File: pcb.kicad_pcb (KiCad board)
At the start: 2 copper layers, 40.6 x 40.6 mm, 3 parts

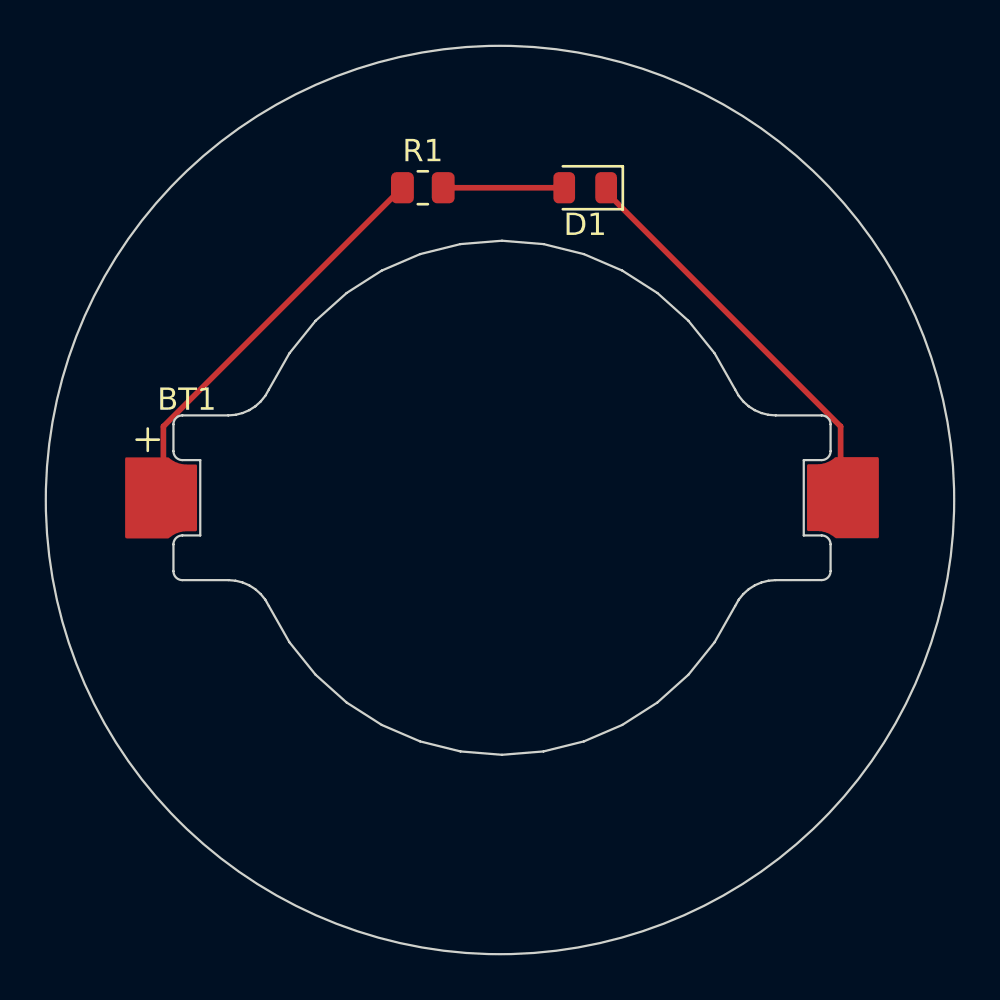
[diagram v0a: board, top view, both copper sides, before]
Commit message: hopefully fix example :/
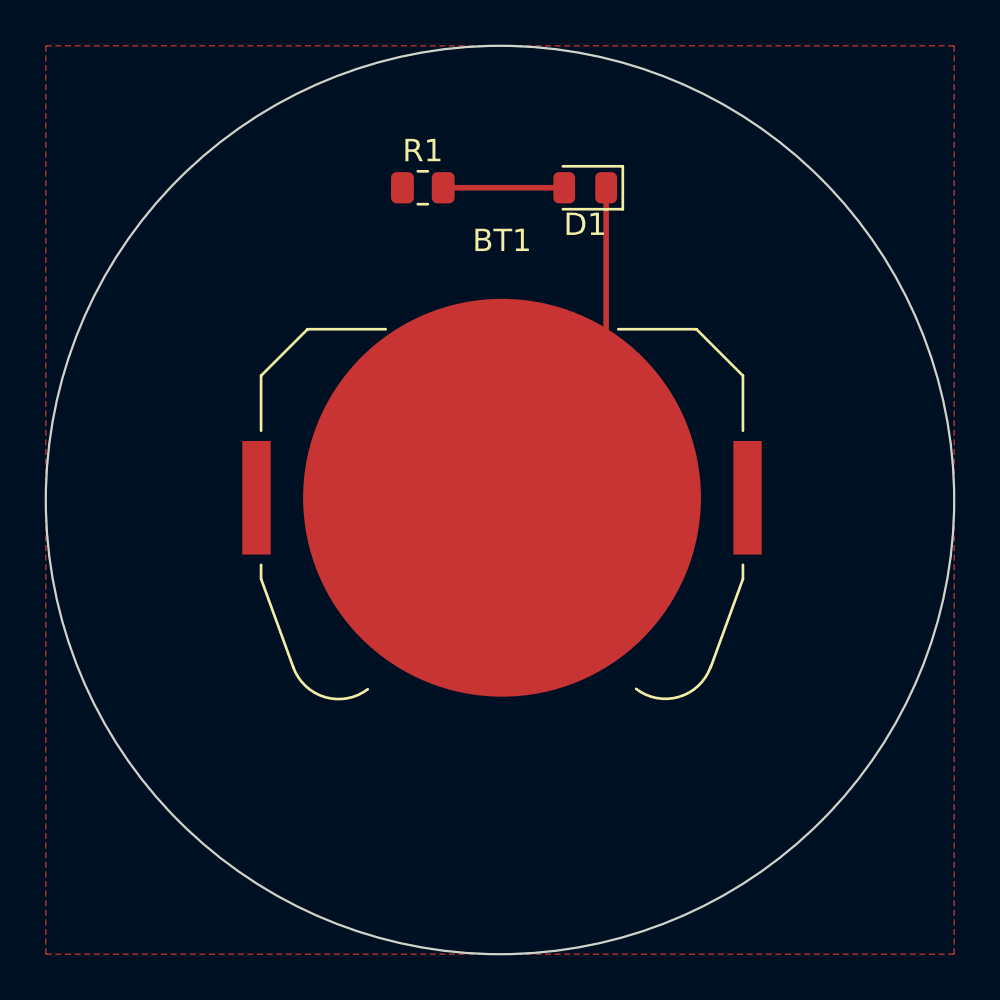
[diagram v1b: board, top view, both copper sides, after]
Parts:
- BT1: footprint Battery:BatteryHolder_Keystone_1057_1x2032 -> Battery:BatteryHolder_Keystone_3034_1x20mm
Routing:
- net Net-(BT1-+): track 18.2 -> 0.00 mm
- net GND: track 18.1 -> 15.6 mm
- added copper zone on F.Cu, net Net-(BT1-+)
